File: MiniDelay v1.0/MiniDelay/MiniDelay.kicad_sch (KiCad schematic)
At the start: 53 parts, among them J1 IDC_2x05, U1 TL074, U2 PT2399, U3 L7805

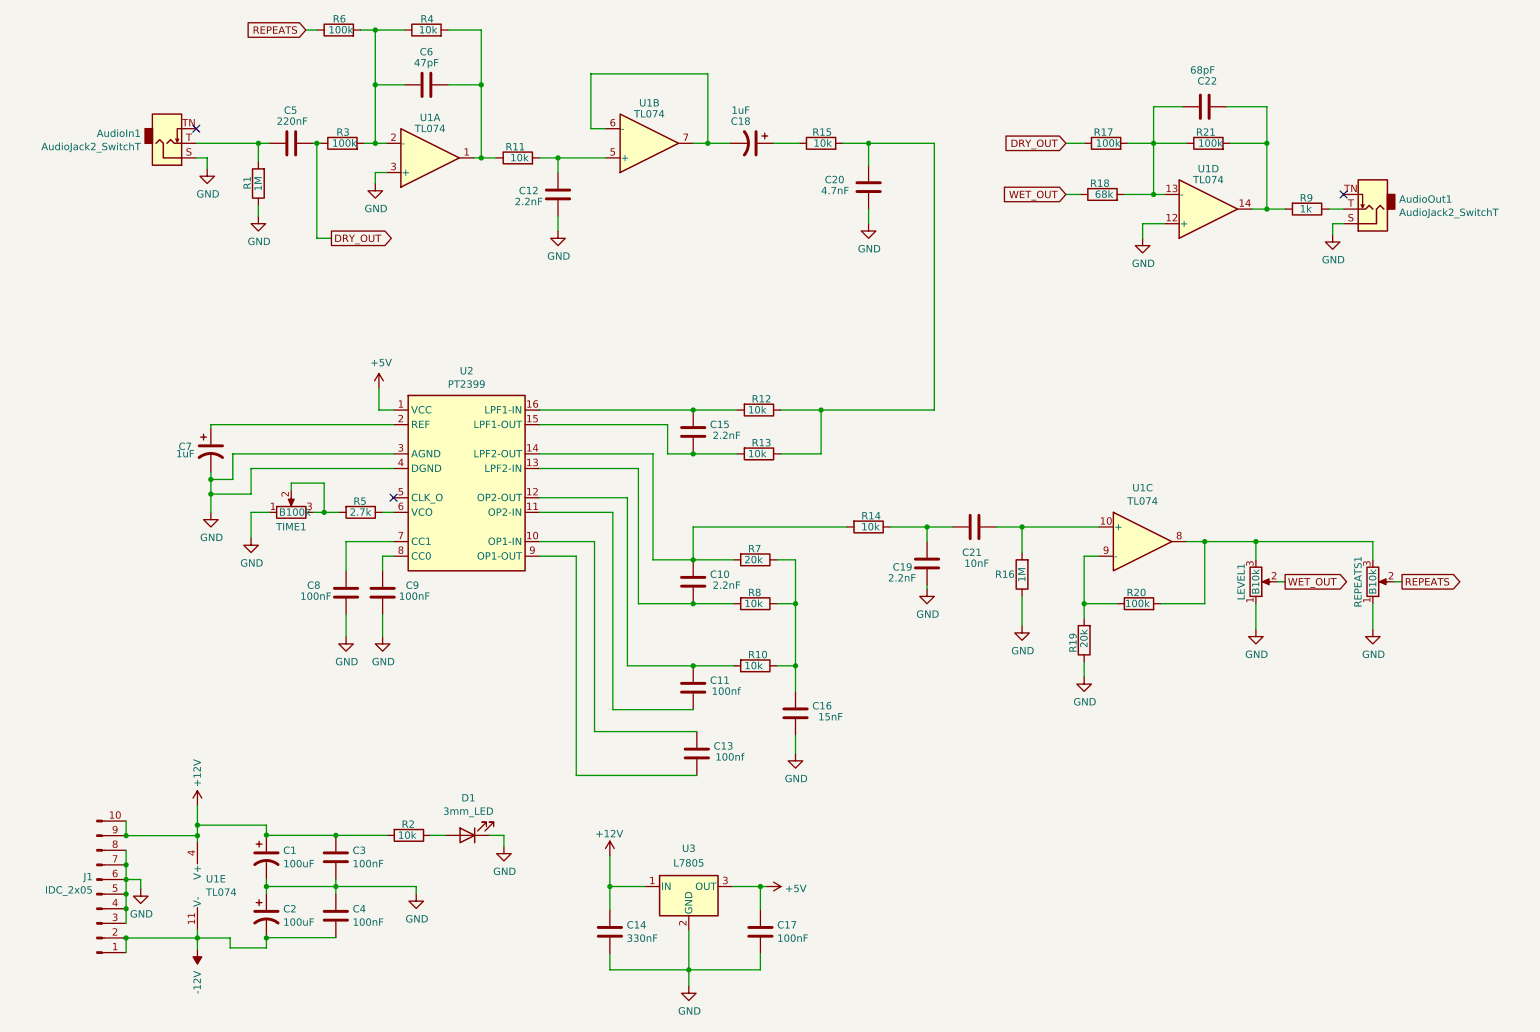
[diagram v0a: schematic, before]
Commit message: Moved everything to SMD
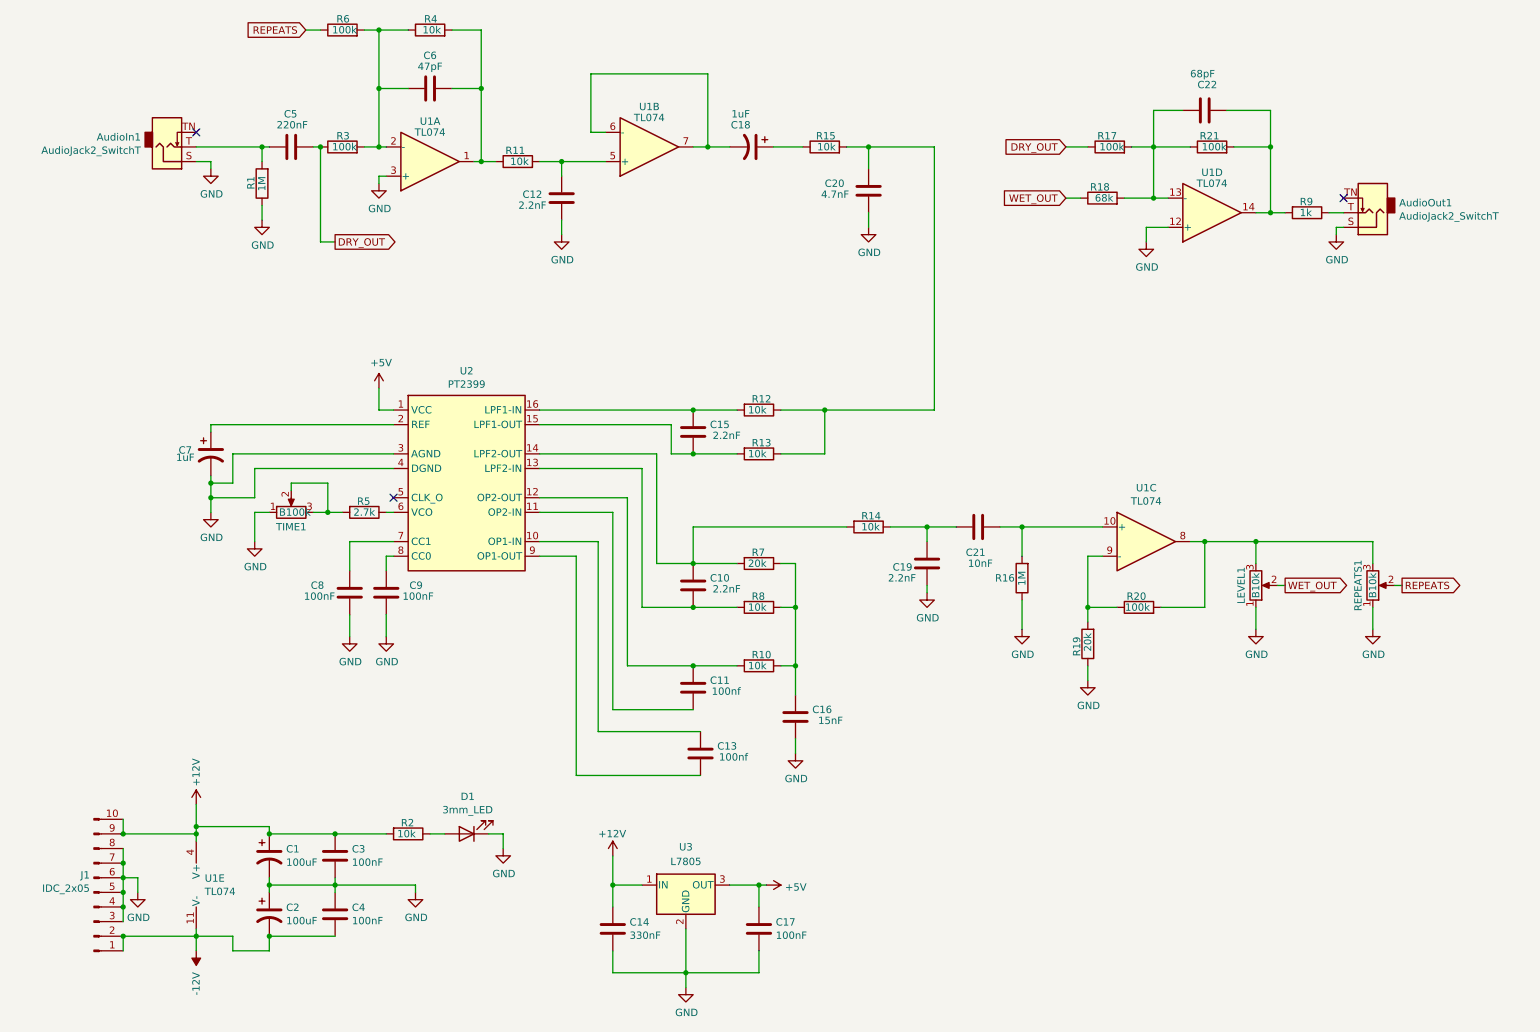
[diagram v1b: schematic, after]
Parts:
- U2: footprint Package_DIP:DIP-16_W7.62mm_Socket_LongPads -> Package_SO:SOP-16_4.55x10.3mm_P1.27mm
- U3: footprint Package_TO_SOT_SMD:TO-263-3_TabPin2 -> Package_TO_SOT_THT:TO-220-3_Vertical
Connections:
- net +12V: now also C1.1, C3.1, R2.2
- net -12V: now also C2.2, C4.2
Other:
- moved on the sheet: AudioIn1, AudioOut1, C1, C10, C12, C13, C14, C16, C17, C18, C2, C20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

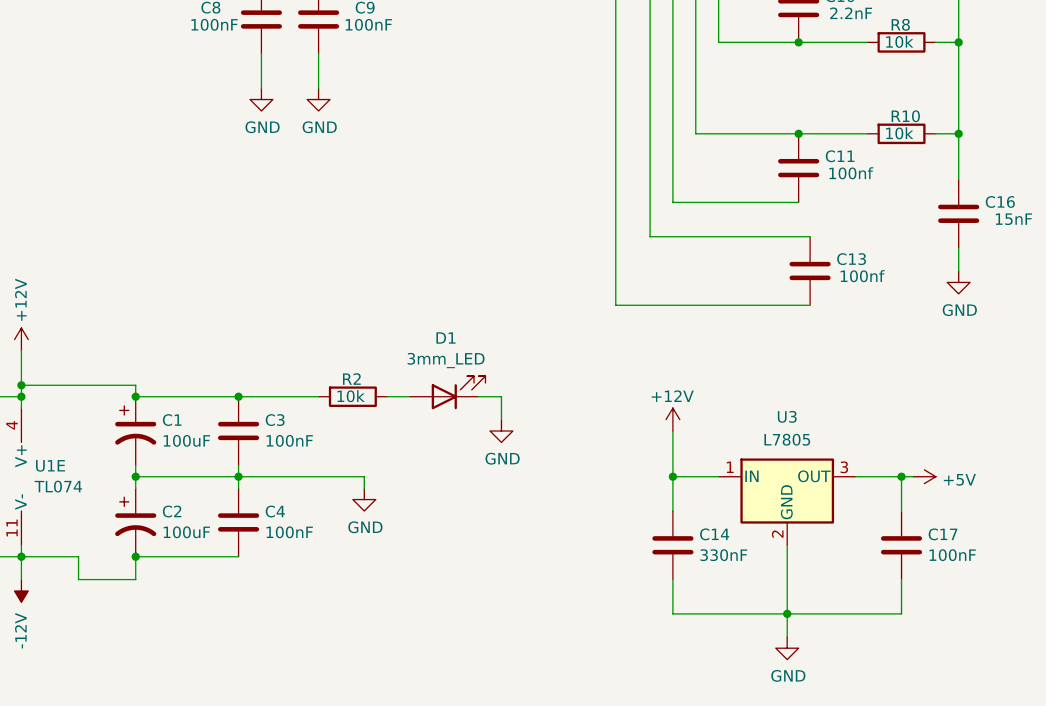
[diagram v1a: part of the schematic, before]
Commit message: Updated bom using LCSC
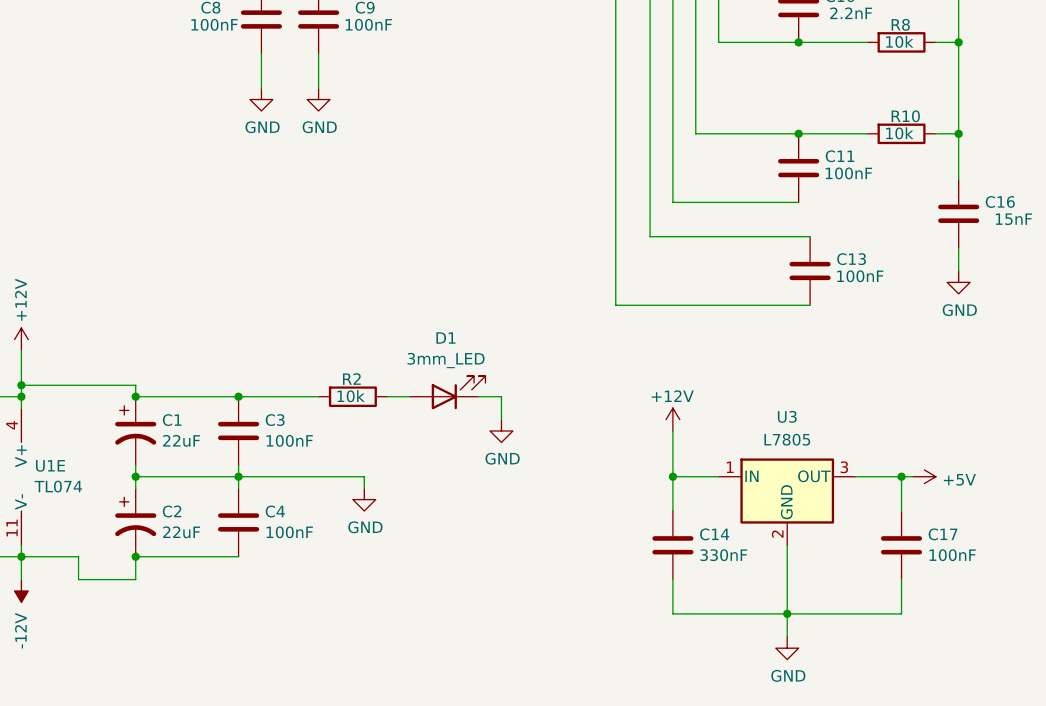
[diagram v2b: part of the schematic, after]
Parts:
- C1, C2: value 100uF -> 22uF; footprint Capacitor_SMD:CP_Elec_4x3.9 -> Capacitor_SMD:C_0805_2012Metric_Pad1.18x1.45mm_HandSolder; LCSC Part # (none) -> C49678; Mfg # (none) -> CC0805KRX7R9BB104
- C10, C12, C15, C19: LCSC Part # (none) -> C107043; Mfg # (none) -> CC0603JRNPO9BN222
- C11, C13: value 100nf -> 100nF; LCSC Part # (none) -> C91183; Mfg # (none) -> CC0603JRX7R9BB104
- C14: LCSC Part # (none) -> C107070; Mfg # (none) -> CC0603KRX7R8BB334
- C16: LCSC Part # (none) -> C2210963; Mfg # (none) -> AC0603KRX7R0BB153
- C17, C3, C4, C8, C9: LCSC Part # (none) -> C91183; Mfg # (none) -> CC0603JRX7R9BB104
- C18, C7: footprint Capacitor_SMD:CP_Elec_4x3.9 -> Capacitor_SMD:C_0603_1608Metric_Pad1.08x0.95mm_HandSolder; LCSC Part # (none) -> C105174; Mfg # (none) -> UMK107AB7105KA-T
- C20: LCSC Part # (none) -> C115060; Mfg # (none) -> CC0603JRX7R9BB472
- C21: LCSC Part # (none) -> C115056; Mfg # (none) -> CC0603JRX7R9BB103
- C22: LCSC Part # (none) -> C519457; Mfg # (none) -> CC0603GRNPO9BN680
- C5: LCSC Part # (none) -> C97857; Mfg # (none) -> GCM188R71H224KA64D
- C6: LCSC Part # (none) -> C105622; Mfg # (none) -> CC0603JRNPO9BN470
- R1, R16: LCSC Part # (none) -> C105578; Mfg # (none) -> RC0603FR-071ML
- R10, R11, R12, R13, R14, R15, R2, R4, R8: LCSC Part # (none) -> C116677; Mfg # (none) -> AC0603FR-0710KL
- R17, R20, R21, R3, R6: LCSC Part # (none) -> C14675; Mfg # (none) -> RC0603FR-07100KL
- R18: LCSC Part # (none) -> C114633; Mfg # (none) -> RC0603FR-0768KL
- R19, R7: LCSC Part # (none) -> C105575; Mfg # (none) -> RC0603FR-0720KL
- R5: LCSC Part # (none) -> C114612; Mfg # (none) -> RC0603FR-072K7L
- R9: LCSC Part # (none) -> C22548; Mfg # (none) -> RC0603FR-071KL
- U1: LCSC Part # (none) -> C107644; Mfg # (none) -> TL074IDT
- U2: LCSC Part # (none) -> C126407; Mfg # (none) -> PT2399-SN
- U3: LCSC Part # (none) -> C347289

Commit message: Worked on BOM
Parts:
- AudioIn1, AudioOut1, J1: Type (none) -> Thru-hole
- C1, C2: Manufacturers Name (none) -> YAGEO; Manufacturers Part Number (none) -> CC0805KRX7R9BB104; Package (none) -> 0805; Type (none) -> Surface mount
- C10, C12, C15, C19: Manufacturers Name (none) -> YAGEO; Manufacturers Part Number (none) -> CC0603JRNPO9BN222; Package (none) -> 0603; Type (none) -> Surface mount
- C11, C13, C17, C3, C4, C8, C9: Manufacturers Name (none) -> YAGEO; Manufacturers Part Number (none) -> CC0603JRX7R9BB104; Package (none) -> 0603; Type (none) -> Surface mount
- C14: Manufacturers Name (none) -> YAGEO; Manufacturers Part Number (none) -> CC0603KRX7R8BB334; Package (none) -> 0603; Type (none) -> Surface mount
- C16: Manufacturers Name (none) -> YAGEO; Manufacturers Part Number (none) -> AC0603KRX7R0BB153; Package (none) -> 0603; Type (none) -> Surface mount
- C18, C7: Manufacturers Name (none) -> Taiyo Yuden; Manufacturers Part Number (none) -> UMK107AB7105KA-T; Package (none) -> 0603; Type (none) -> Surface mount
- C20: Manufacturers Name (none) -> YAGEO; Manufacturers Part Number (none) -> CC0603JRX7R9BB472; Package (none) -> 0603; Type (none) -> Surface mount
- C21: Manufacturers Name (none) -> YAGEO; Manufacturers Part Number (none) -> CC0603JRX7R9BB103; Package (none) -> 0603; Type (none) -> Surface mount
- C22: Manufacturers Name (none) -> YAGEO; Manufacturers Part Number (none) -> CC0603GRNPO9BN680; Package (none) -> 0603; Type (none) -> Surface mount
- C5: Manufacturers Name (none) -> Murata Electronics; Manufacturers Part Number (none) -> GCM188R71H224KA64D; Package (none) -> 0603; Type (none) -> Surface mount
- C6: Manufacturers Name (none) -> YAGEO; Manufacturers Part Number (none) -> CC0603JRNPO9BN470; Package (none) -> 0603; Type (none) -> Surface mount
- D1: LCSC Part # (none) -> C2856645; Manufacturers Name (none) -> EKINGLUX; Manufacturers Part Number (none) -> EL304RD; Mfg # (none) -> EL304RD; Type (none) -> Thru-hole
- LEVEL1, REPEATS1, TIME1: Manufacturers Part Number (none) -> RK097N; Mfg # (none) -> RK097N; Type (none) -> Thru-hole
- R1, R16: Manufacturers Name (none) -> YAGEO; Manufacturers Part Number (none) -> RC0603FR-071ML; Package (none) -> 0603; Type (none) -> Surface mount
- R10, R11, R12, R13, R14, R15, R2, R4, R8: Manufacturers Name (none) -> YAGEO; Manufacturers Part Number (none) -> AC0603FR-0710KL; Package (none) -> 0603; Type (none) -> Surface mount
- R17, R20, R21, R3, R6: Manufacturers Name (none) -> YAGEO; Manufacturers Part Number (none) -> RC0603FR-07100KL; Package (none) -> 0603; Type (none) -> Surface mount
- R18: Manufacturers Name (none) -> YAGEO; Manufacturers Part Number (none) -> RC0603FR-0768KL; Package (none) -> 0603; Type (none) -> Surface mount
- R19, R7: Manufacturers Name (none) -> YAGEO; Manufacturers Part Number (none) -> RC0603FR-0720KL; Package (none) -> 0603; Type (none) -> Surface mount
- R5: Manufacturers Name (none) -> YAGEO; Manufacturers Part Number (none) -> RC0603FR-072K7L; Package (none) -> 0603; Type (none) -> Surface mount
- R9: Manufacturers Name (none) -> YAGEO; Manufacturers Part Number (none) -> RC0603FR-071KL; Package (none) -> 0603; Type (none) -> Surface mount
- U1: Manufacturers Name (none) -> STMicroelectronics; Manufacturers Part Number (none) -> TL074IDT; Package (none) -> SOIC-14_150mil; Type (none) -> Surface mount
- U2: Manufacturers Name (none) -> PTC(Princeton Tech); Manufacturers Part Number (none) -> PT2399-SN; Mfg # PT2399-SN -> PT2399-SN; Package (none) -> SOP-16_150mil; Type (none) -> Surface mount
- U3: footprint Package_TO_SOT_THT:TO-220-3_Vertical -> Package_TO_SOT_SMD:TO-252-2; LCSC Part # C347289 -> C310413; Manufacturers Name (none) -> STMicroelectronics; Manufacturers Part Number (none) -> L7805CDT-TR; Mfg # (none) -> L7805CDT-TR; Package (none) -> TO-252-3; Type (none) -> Surface mount
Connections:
- net GND: now also U1.10 (+), U1.5 (+); no longer U1.12 (+), U1.3 (+)
- net at C22.1, R21.2, R9.2: now also U1.7; no longer U1.14
- net at C6.1, R11.1, R4.2: now also U1.8; no longer U1.1
- net at C12.2, R11.2: now also U1.12 (+); no longer U1.5 (+)
- net at C6.2, R3.2, R4.1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: now also U1.9 (-); no longer U1.2 (-)
- net at C21.2, R16.2: now also U1.3 (+); no longer U1.10 (+)
- net at R19.2, R20.1: now also U1.2 (-); no longer U1.9 (-)
- net at LEVEL1.3, R20.2, REPEATS1.3: now also U1.1; no longer U1.8
- net at C22.2, R17.2, R18.2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: now also U1.6 (-); no longer U1.13 (-)
- new net: C18.2, U1.13 (-), U1.14
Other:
- company: (none) -> benjiaomodular
- title: (none) -> MiniDelay
- moved on the sheet: U1A, U1B, U1C, U1D

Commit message: Complete BOM
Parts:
- AudioIn1, AudioOut1: Manufacturers Name (none) -> Tayda Electronics; Manufacturers Part Number (none) -> PJ-3001F; Mfg # (none) -> PJ-3001F; Part Description (none) -> PJ-3001F 3.5mm Mono Phone Jack
- J1: LCSC Part # (none) -> C706914; Manufacturers Name (none) -> XKB Connectivity; Manufacturers Part Number (none) -> X9555WV-2X05-6TV01; Mfg # (none) -> X9555WV-2X05-6TV01
- LEVEL1, REPEATS1: Manufacturers Name (none) -> Alpha (Taiwan); Manufacturers Part Number RK097N -> RD901F-40-15R1-B10K; Mfg # RK097N -> RD901F-40-15R1-B10K; Part Description (none) -> 10K OHM Linear Taper Potentiometer Round Shaft PCB 9mm
- TIME1: Manufacturers Name (none) -> Alpha (Taiwan); Manufacturers Part Number RK097N -> RD901F-40-15F-B100K; Mfg # RK097N -> RD901F-40-15F-B100K; Part Description (none) -> 100K OHM Linear Taper Potentiometer D Shaft PCB 9mm
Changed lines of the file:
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@@
+      (effects (font (size 1.27 1.27)) hide)
+    )
+    (property "Manufacturers Name" "Tayda Electronics" (id 5) (at 38.1 41.91 0)
+      (effects (font (size 1.27 1.27)) hide)
+    )
+    (property "Manufacturers Part Number" "PJ-3001F" (id 6) (at 38.1 41.91 0)
+      (effects (font (size 1.27 1.27)) hide)
+    )
+    (property "Mfg #" "PJ-3001F" (id 7) (at 38.1 41.91 0)
+      (effects (font (size 1.27 1.27)) hide)
+    )
+    (property "Part Description" "PJ-3001F 3.5mm Mono Phone Jack" (id 8) (at 38.1 41.91 0)
       (effects (font (size 1.27 1.27)) hide)
     )
@@
     )
     (property "Type" "Thru-hole" (id 4) (at 247.65 53.34 0)
+      (effects (font (size 1.27 1.27)) hide)
+    )
+    (property "Manufacturers Name" "Tayda Electronics" (id 5) (at 247.65 53.34 0)
+      (effects (font (size 1.27 1.27)) hide)
+    )
+    (property "Manufacturers Part Number" "PJ-3001F" (id 6) (at 247.65 53.34 0)
+      (effects (font (size 1.27 1.27)) hide)
+    )
+    (property "Mfg #" "PJ-3001F" (id 7) (at 247.65 53.34 0)
+      (effects (font (size 1.27 1.27)) hide)
+    )
+    (property "Part Description" "PJ-3001F 3.5mm Mono Phone Jack" (id 8) (at 247.65 53.34 0)
       (effects (font (size 1.27 1.27)) hide)
     )
@@
       (effects (font (size 1.27 1.27)) hide)
     )
-    (property "Manufacturers Part Number" "RK097N" (id 5) (at 59.69 105.41 0)
-      (effects (font (size 1.27 1.27)) hide)
-    )
-    (property "Mfg #" "RK097N" (id 6) (at 59.69 105.41 0)
+    (property "Manufacturers Part Number" "RD901F-40-15F-B100K" (id 5) (at 59.69 105.41 0)
+      (effects (font (size 1.27 1.27)) hide)
+    )
+    (property "Mfg #" "RD901F-40-15F-B100K" (id 6) (at 59.69 105.41 0)
+      (effects (font (size 1.27 1.27)) hide)
+    )
+    (property "Manufacturers Name" "Alpha (Taiwan)" (id 7) (at 59.69 105.41 0)
+      (effects (font (size 1.27 1.27)) hide)
+    )
+    (property "Part Description" "100K OHM Linear Taper Potentiometer D Shaft PCB 9mm" (id 8) (at 59.69 105.41 0)
       (effects (font (size 1.27 1.27)) hide)
     )
@@
       (effects (font (size 1.27 1.27)) hide)
     )
-    (property "Manufacturers Part Number" "RK097N" (id 5) (at 247.65 118.11 0)
-      (effects (font (size 1.27 1.27)) hide)
-    )
-    (property "Mfg #" "RK097N" (id 6) (at 247.65 118.11 0)
+    (property "Manufacturers Part Number" "RD901F-40-15R1-B10K" (id 5) (at 247.65 118.11 0)
+      (effects (font (size 1.27 1.27)) hide)
+    )
+    (property "Mfg #" "RD901F-40-15R1-B10K" (id 6) (at 247.65 118.11 0)
+      (effects (font (size 1.27 1.27)) hide)
+    )
+    (property "Manufacturers Name" "Alpha (Taiwan)" (id 7) (at 247.65 118.11 0)
+      (effects (font (size 1.27 1.27)) hide)
+    )
+    (property "Part Description" "10K OHM Linear Taper Potentiometer Round Shaft PCB 9mm" (id 8) (at 247.65 118.11 0)
       (effects (font (size 1.27 1.27)) hide)
     )
@@
       (effects (font (size 1.27 1.27)) hide)
     )
-    (property "Datasheet" "" (id 3) (at 218.44 35.56 0)
+    (property "Datasheet" "~" (id 3) (at 218.44 35.56 0)
       (effects (font (size 1.27 1.27)) hide)
     )
@@
       (effects (font (size 1.27 1.27)) hide)
     )
-    (property "Manufacturers Part Number" "RK097N" (id 5) (at 227.33 118.11 0)
-      (effects (font (size 1.27 1.27)) hide)
-    )
-    (property "Mfg #" "RK097N" (id 6) (at 227.33 118.11 0)
+    (property "Manufacturers Part Number" "RD901F-40-15R1-B10K" (id 5) (at 227.33 118.11 0)
+      (effects (font (size 1.27 1.27)) hide)
+    )
+    (property "Mfg #" "RD901F-40-15R1-B10K" (id 6) (at 227.33 118.11 0)
+      (effects (font (size 1.27 1.27)) hide)
+    )
+    (property "Manufacturers Name" "Alpha (Taiwan)" (id 7) (at 227.33 118.11 0)
+      (effects (font (size 1.27 1.27)) hide)
+    )
+    (property "Part Description" "10K OHM Linear Taper Potentiometer Round Shaft PCB 9mm" (id 8) (at 227.33 118.11 0)
       (effects (font (size 1.27 1.27)) hide)
     )
@@
       (effects (font (size 1.27 1.27)) hide)
     )
+    (property "LCSC Part #" "C706914" (id 5) (at 25.4 171.45 0)
+      (effects (font (size 1.27 1.27)) hide)
+    )
+    (property "Manufacturers Name" "XKB Connectivity " (id 6) (at 25.4 171.45 0)
+      (effects (font (size 1.27 1.27)) hide)
+    )
+    (property "Manufacturers Part Number" "X9555WV-2X05-6TV01" (id 7) (at 25.4 171.45 0)
+      (effects (font (size 1.27 1.27)) hide)
+    )
+    (property "Mfg #" "X9555WV-2X05-6TV01" (id 8) (at 25.4 171.45 0)
+      (effects (font (size 1.27 1.27)) hide)
+    )
